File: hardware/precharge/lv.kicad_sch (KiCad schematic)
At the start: 27 parts, among them K2 G5Q-1EU DC12, K3 G5Q-1EU DC12, Q6 XP262N7002TR-G, Q7 XP262N7002TR-G, Q8 XP262N7002TR-G, U5 40106, U6 LM339, U7 4013, U8 4001

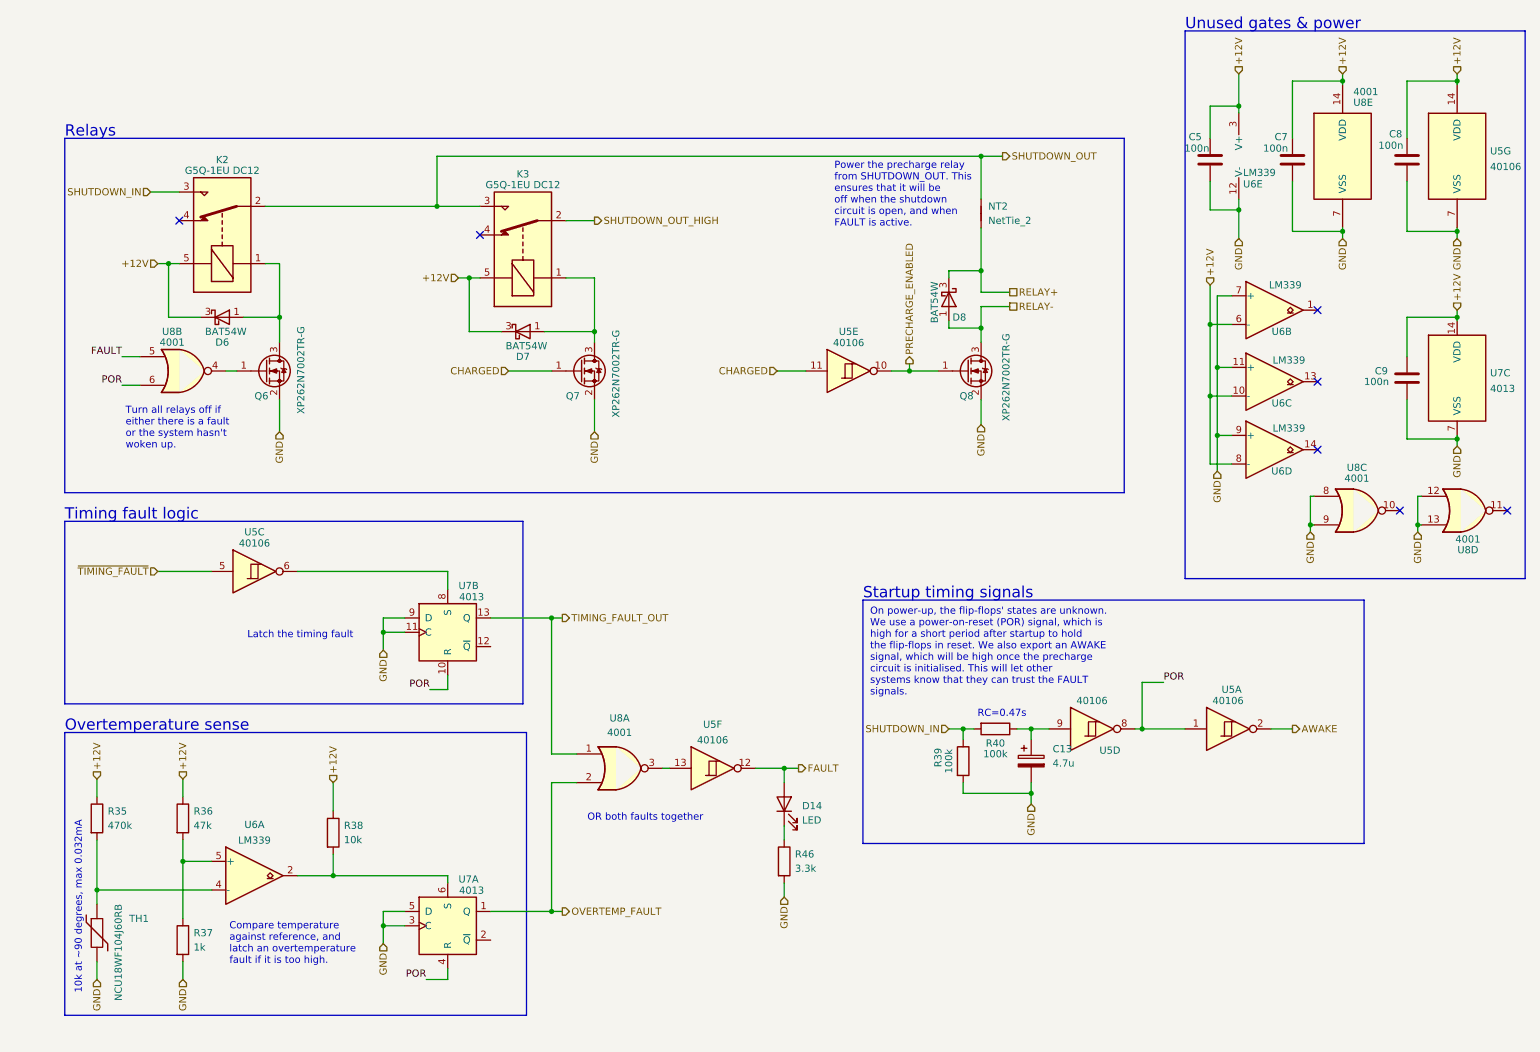
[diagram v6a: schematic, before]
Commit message: Added support for TS_ACTIVE signal, adjusted resistor divider
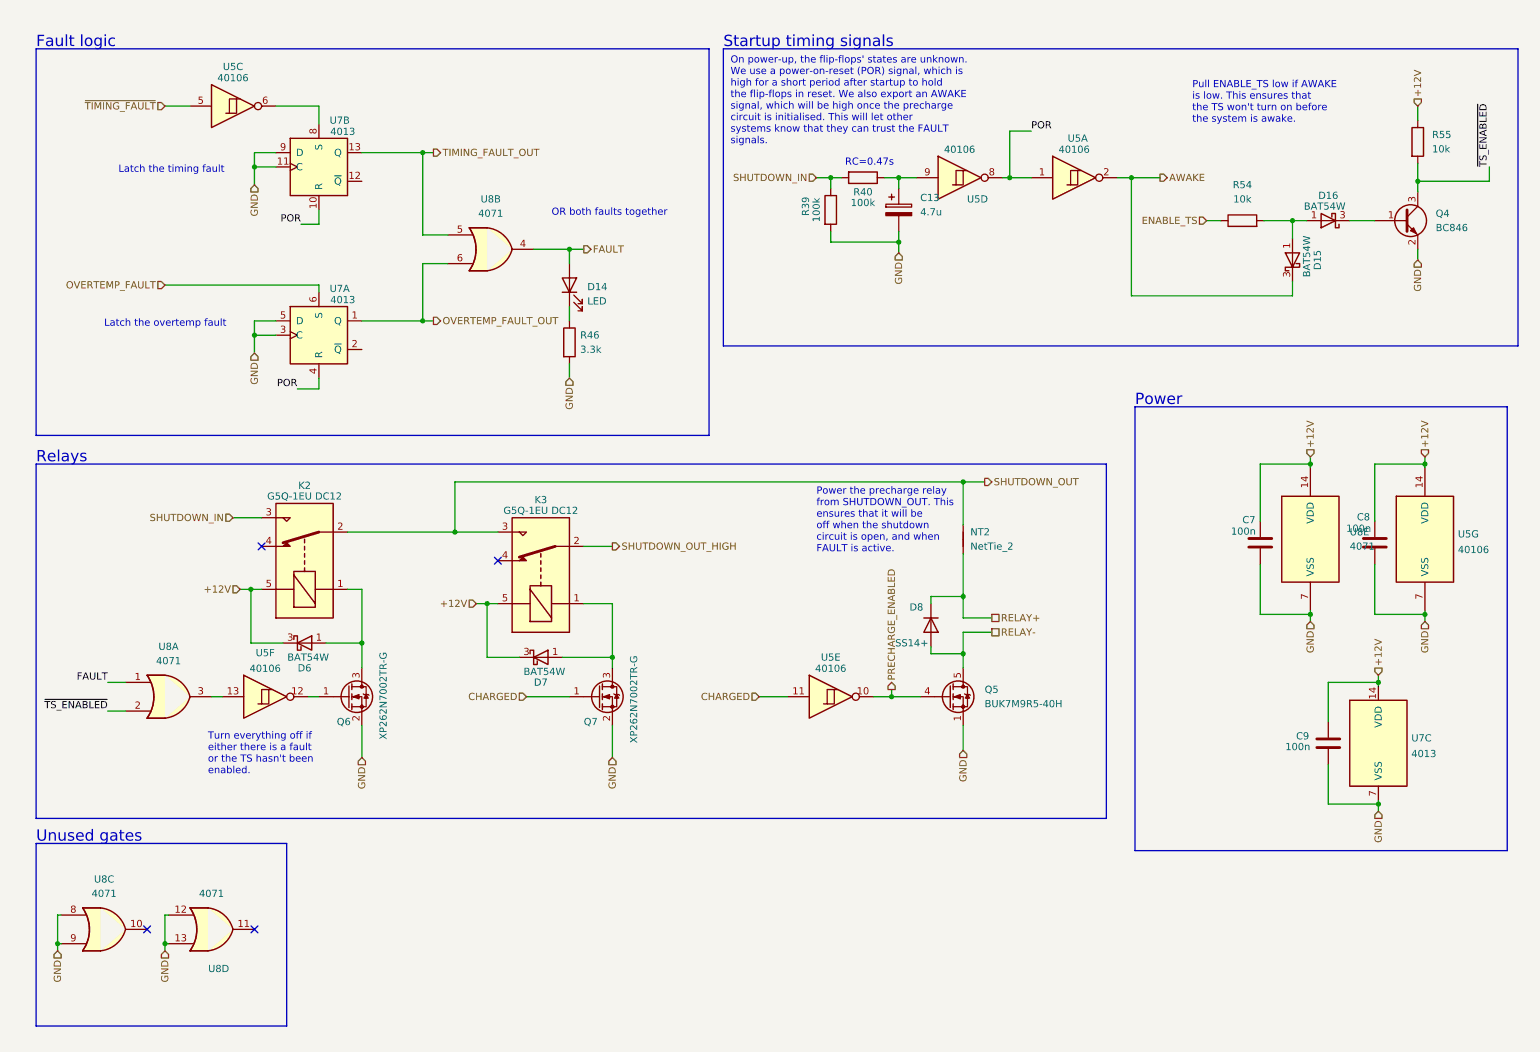
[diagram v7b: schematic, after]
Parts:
- removed C5: 100n, Capacitor_SMD:C_0603_1608Metric, symbol Device:C
- removed D8: BAT54W, Package_TO_SOT_SMD:SOT-323_SC-70, symbol Diode:BAT54W
- removed Q8: XP262N7002TR-G, Package_TO_SOT_SMD:SOT-23, symbol Device:Q_NMOS_GSD
- removed R35: 470k, Resistor_SMD:R_0603_1608Metric, symbol Device:R
- removed R36: 47k, Resistor_SMD:R_0603_1608Metric, symbol Device:R
- removed R37: 1k, Resistor_SMD:R_0603_1608Metric, symbol Device:R
- removed R38: 10k, Resistor_SMD:R_0603_1608Metric, symbol Device:R
- removed TH1: NCU18WF104J60RB, Resistor_SMD:R_0603_1608Metric, symbol Device:Thermistor
- removed U6: LM339, Package_SO:SOIC-14_3.9x8.7mm_P1.27mm, symbol Comparator:LM339
- removed U8: 4001, Package_SO:SOIC-14_3.9x8.7mm_P1.27mm, symbol 4xxx:4001
- added D15, D16: BAT54W, Package_TO_SOT_SMD:SOT-323_SC-70, symbol Diode:BAT54W
- added D8: SS14+, Diode_SMD:D_SMA, symbol Device:D
- added Q4: BC846, Package_TO_SOT_SMD:SOT-23, symbol Transistor_BJT:BC846
- added Q5: BUK7M9R5-40H, Package_TO_SOT_SMD:LFPAK33, symbol Transistor_FET:BUK7M9R9-60EX
- added R54, R55: 10k, Resistor_SMD:R_0603_1608Metric, symbol Device:R
- added U8: 4071, Package_SO:SOIC-14_3.9x8.7mm_P1.27mm, symbol 4xxx:4071
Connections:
- net +12V: now also R55.1, U8.14 (VDD)
- net AWAKE: now also D15.3 (K)
- net FAULT: now also U8.1, U8.4; no longer U5.12
- net GND: now also Q4.2 (E), Q5.1 (S), Q5.2 (S), Q5.3 (S), U8.12, U8.13, U8.7 (VSS), U8.8, U8.9
- net OVERTEMP_FAULT: now also U7.6 (S); no longer U7.1 (Q)
- net PRECHARGE_ENABLED: now also Q5.4 (G)
- net RELAY+: now also D8.1 (K)
- net RELAY-: now also D8.2 (A), Q5.5 (D)
- net TIMING_FAULT_OUT: now also U8.5
- net at Q6.1 (G): now also U5.12
- net at U5.13: now also U8.3
- new net: D15.1 (A), D16.1 (A), R54.2
- new net: D16.3 (K), Q4.1 (B)
- new net ENABLE_TS: R54.1
- new net OVERTEMP_FAULT_OUT: U7.1 (Q), U8.6
- new net ~{TS_ENABLED}: Q4.3 (C), R55.2, U8.2
- no-connect marks 7 -> 4
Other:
- note added: "Fault logic"
- note added: "Latch the overtemp fault"
- note added: "Power"
- note added: "Pull ENABLE_TS low if AWAKE is low. This ensures that the TS won't turn on before the system is awake."
- note added: "Turn everything off if either there is a fault or the TS hasn't been enabled."
- note added: "Unused gates"
- note removed: "10k at ~90 degrees, max 0.032mA"
- note removed: "Compare temperature against reference, and latch an overtemperature fault if it is too high."
- note removed: "Overtemperature sense"
- note removed: "Timing fault logic"
- note removed: "Turn all relays off if either there is a fault or the system hasn't woken up."
- note removed: "Unused gates & power"
- moved on the sheet: C13, C7, C8, C9, D14, D6, D7, K2, K3, NT2, Q6, Q7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

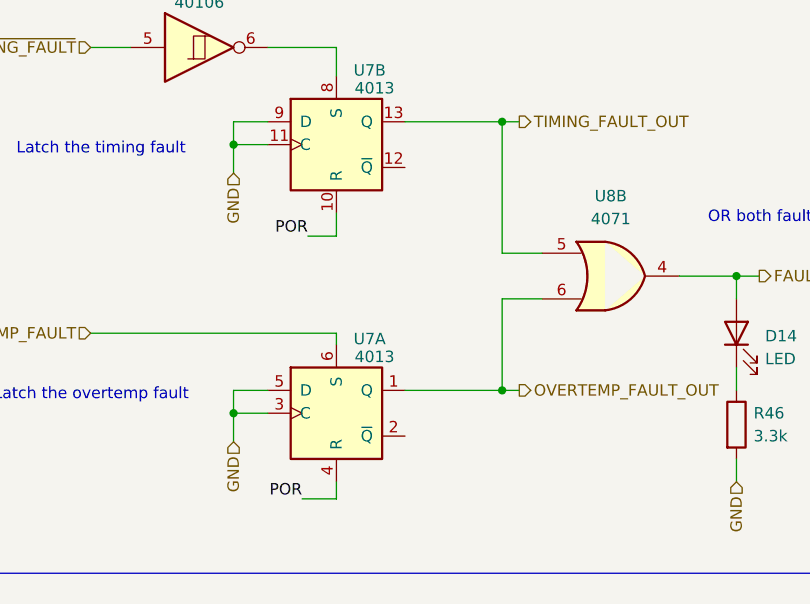
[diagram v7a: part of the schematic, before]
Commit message: Added precharge layout
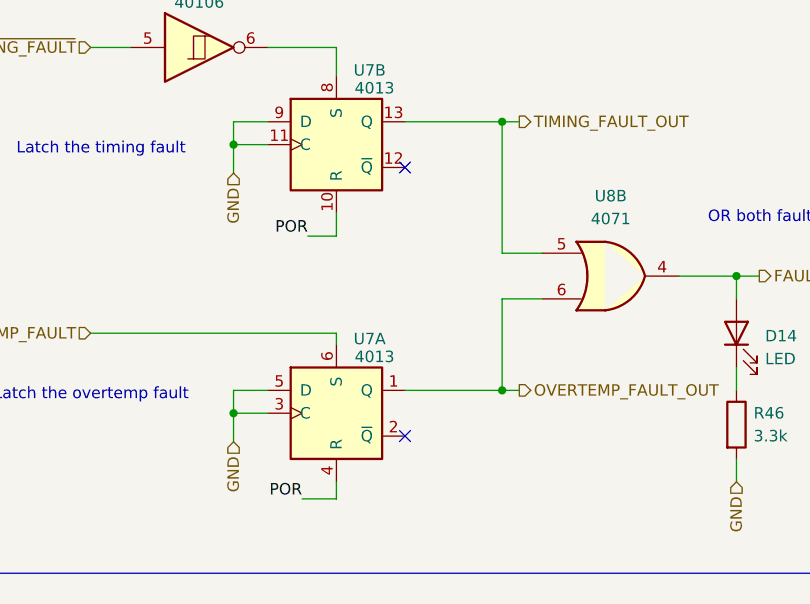
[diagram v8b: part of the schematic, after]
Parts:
- K2, K3: footprint Relay_THT:Relay_SPDT_Omron-G5Q-1 -> footprints:PCH-112L2MH
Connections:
- no-connect marks 4 -> 6
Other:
- title: (none) -> Precharge LV Side
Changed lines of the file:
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@@
 (kicad_sch (version 20211123) (generator eeschema)
   (paper "A4")
+  (title_block
+    (title "Precharge LV Side")
+  )
   (junction (at 75.565 125.095) (diameter 0) (color 0 0 0 0)
   )
@@
   )
   (no_connect (at 99.695 110.49))
+  (no_connect (at 75.565 43.18))
+  (no_connect (at 75.565 73.025))
   (no_connect (at 57.785 107.95))
   (no_connect (at 37.465 175.895))
@@
     (property "Reference" "K2" (id 0) (at 65.405 97.155 90))
     (property "Value" "G5Q-1EU DC12" (id 1) (at 65.405 99.06 90))
-    (property "Footprint" "Relay_THT:Relay_SPDT_Omron-G5Q-1" (id 2) (at 66.675 99.06 0)
+    (property "Footprint" "footprints:PCH-112L2MH" (id 2) (at 66.675 99.06 0)
       (effects (font (size 1.27 1.27)) (justify left) hide)
     )
@@
     (property "Reference" "K3" (id 0) (at 107.315 99.695 90))
     (property "Value" "G5Q-1EU DC12" (id 1) (at 107.315 101.6 90))
-    (property "Footprint" "Relay_THT:Relay_SPDT_Omron-G5Q-1" (id 2) (at 108.585 101.6 0)
+    (property "Footprint" "footprints:PCH-112L2MH" (id 2) (at 108.585 101.6 0)
       (effects (font (size 1.27 1.27)) (justify left) hide)
     )
